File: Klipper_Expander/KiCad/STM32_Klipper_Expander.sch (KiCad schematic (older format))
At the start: 45 parts, among them J1 USB_B_Micro, J10 Conn_01x01, J11 Conn_01x03, J12 Conn_01x02, J2 Conn_01x04, J4 Conn_01x03, J5 Vin, J6 Screw_Terminal_01x08, J7 Conn_01x02, J8 Conn_01x02, J9 Conn_01x02, Q1 IRLML6344TRPBF, Q2 IRLML6344TRPBF, Q3 IRLML6344TRPBF, Q4 IRLML6344TRPBF, SW2 SW_SPST, U1 STM32F042F6Px, U2 AP2127K-3.3, U3 74LVC1G17

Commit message: Status LED's and silkscren adjustments.
Added status LED's for Vin (12/24V), USB (5V), and all 4 mosfets on the drain. LED's will signal mosfet output status.

Gerber and PNP files still need to be completed.
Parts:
- added D2, D3, D4, D5, D6, D7: LED, LED_SMD:LED_0805_2012Metric, symbol Device:LED
- added R15, R18, R19, R20, R22: 4.7K, Resistor_SMD:R_0805_2012Metric, symbol Device:R
- added R21: 1K, Resistor_SMD:R_0805_2012Metric, symbol Device:R
- J12: value Conn_01x02 -> Conn_01x03; footprint Connector_PinHeader_2.54mm:PinHeader_1x02_P2.54mm_Vertical -> Connector_PinHeader_2.54mm:PinHeader_1x03_P2.54mm_Vertical; symbol Connector_Generic:Conn_01x02 -> Connector_Generic:Conn_01x03
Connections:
- wire segments 140 -> 168

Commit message: Updated Gerber and Production files, Minor changes
Changed thermsitor pullups to 4K7 to increse range and reliability.
Added silkscreen to indicate what the status LED's are showing.
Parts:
- R16, R17: value 10K -> 4.7K; LCSC C17414 -> C17673; MPN RC0805JR-0710KL -> RC0805JR-074K7L; SKU 301010361 -> 301010306
- U3: footprint Package_TO_SOT_SMD:SOT-353_SC-70-5 -> digikey-footprints:SOT-753; LCSC C124293 -> C6076; MPN 74LVC1G17SE-7 -> (none)
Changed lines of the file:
@@
 F 0 "U3" H 5350 4000 50  0000 C CNN
 F 1 "74LVC1G17" H 5250 3650 50  0000 C CNN
-F 2 "Package_TO_SOT_SMD:SOT-353_SC-70-5" H 5550 3800 50  0001 C CNN
+F 2 "digikey-footprints:SOT-753" H 5550 3800 50  0001 C CNN
 F 3 "http://www.ti.com/lit/sg/scyt129e/scyt129e.pdf" H 5550 3800 50  0001 C CNN
-F 4 "C124293" H 5550 3800 50  0001 C CNN "LCSC"
-F 5 "74LVC1G17SE-7" H 5350 4100 50  0001 C CNN "MPN"
+F 4 "C6076" H 5550 3800 50  0001 C CNN "LCSC"
 	1    5550 3800
 	1    0    0    -1
@@
 	1    2650 6350
 	1    0    0    1
-$EndComp
-$Comp
-L Device:R R16
-U 1 1 5E341B23
-P 6750 5550
-F 0 "R16" H 6680 5504 50  0000 R CNN
-F 1 "10K" H 6680 5595 50  0000 R CNN
-F 2 "Resistor_SMD:R_0805_2012Metric" V 6680 5550 50  0001 C CNN
-F 3 "~" H 6750 5550 50  0001 C CNN
-F 4 "C17414" H 6750 5550 50  0001 C CNN "LCSC"
-F 5 "RC0805JR-0710KL" H 6680 5604 50  0001 C CNN "MPN"
-F 6 "301010361" H 6680 5604 50  0001 C CNN "SKU"
-	1    6750 5550
-	0    -1   1    0
-$EndComp
-$Comp
-L Device:R R17
-U 1 1 5E34C47F
-P 8000 5550
-F 0 "R17" H 7930 5504 50  0000 R CNN
-F 1 "10K" H 7930 5595 50  0000 R CNN
-F 2 "Resistor_SMD:R_0805_2012Metric" V 7930 5550 50  0001 C CNN
-F 3 "~" H 8000 5550 50  0001 C CNN
-F 4 "C17414" H 8000 5550 50  0001 C CNN "LCSC"
-F 5 "RC0805JR-0710KL" H 7930 5604 50  0001 C CNN "MPN"
-F 6 "301010361" H 7930 5604 50  0001 C CNN "SKU"
-	1    8000 5550
-	0    -1   1    0
 $EndComp
 $Comp
@@
 	4050 3200 4050 3150
 $Comp
-L power:+3V3 #PWR?
+L power:+3V3 #PWR0110
 U 1 1 5EBA479A
 P 3800 5500
-F 0 "#PWR?" H 3800 5350 50  0001 C CNN
+F 0 "#PWR0110" H 3800 5350 50  0001 C CNN
 F 1 "+3V3" H 3815 5673 50  0000 C CNN
 F 2 "" H 3800 5500 50  0001 C CNN
@@
 Wire Wire Line
 	3800 5600 3800 5500
+$Comp
+L Device:R R16
+U 1 1 5E9F90AA
+P 6750 5550
+F 0 "R16" H 6680 5504 50  0000 R CNN
+F 1 "4.7K" H 6680 5595 50  0000 R CNN
+F 2 "Resistor_SMD:R_0805_2012Metric" V 6680 5550 50  0001 C CNN
+F 3 "~" H 6750 5550 50  0001 C CNN
+F 4 "C17673" H 6750 5550 50  0001 C CNN "LCSC"
+F 5 "RC0805JR-074K7L" H 6750 5550 50  0001 C CNN "MPN"
+F 6 "301010306" H 6750 5550 50  0001 C CNN "SKU"
+	1    6750 5550
+	0    -1   1    0
+$EndComp
+$Comp
+L Device:R R17
+U 1 1 5EA00768
+P 8000 5550
+F 0 "R17" H 7930 5504 50  0000 R CNN
+F 1 "4.7K" H 7930 5595 50  0000 R CNN
+F 2 "Resistor_SMD:R_0805_2012Metric" V 7930 5550 50  0001 C CNN
+F 3 "~" H 8000 5550 50  0001 C CNN
+F 4 "C17673" H 8000 5550 50  0001 C CNN "LCSC"
+F 5 "RC0805JR-074K7L" H 8000 5550 50  0001 C CNN "MPN"
+F 6 "301010306" H 8000 5550 50  0001 C CNN "SKU"
+	1    8000 5550
+	0    -1   1    0
+$EndComp
 $EndSCHEMATC

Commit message: Add interactive BOM and Project Based Library (#12)
* Change from global to Project based library

Project based libraary added which includes all schematic symbols, footprints, and 3D models

* Fixed links to Footprint and Symbol Libraries

* Add interactiveBOM
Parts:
- C1, C2, C3, C4, C5, C6: footprint Capacitor_SMD:C_0805_2012Metric -> KlipperExpander:C_0805_2012Metric; symbol Device:C -> KlipperExpander:C
- D1, D2, D3, D4, D5, D6, D7: footprint LED_SMD:LED_0805_2012Metric -> KlipperExpander:LED_0805_2012Metric; symbol Device:LED -> KlipperExpander:LED
- F1: footprint TRA_KiCad_Footprints:3544-2_FuseHolder -> KlipperExpander:3544-2_FuseHolder; symbol Device:Fuse -> KlipperExpander:Fuse
- H1, H2: footprint MountingHole:MountingHole_3.2mm_M3 -> KlipperExpander:MountingHole_3.2mm_M3
- J1: footprint TRA_KiCad_Footprints:Molex-105017-0001-USBMicroB -> KlipperExpander:Molex-105017-0001-USBMicroB; symbol Connector:USB_B_Micro -> KlipperExpander:USB_B_Micro
- J10: footprint Connector_PinHeader_2.54mm:PinHeader_1x01_P2.54mm_Vertical -> KlipperExpander:PinHeader_1x01_P2.54mm_Vertical; symbol Connector_Generic:Conn_01x01 -> KlipperExpander:Conn_01x01
- J11, J12, J4: footprint Connector_PinHeader_2.54mm:PinHeader_1x03_P2.54mm_Vertical -> KlipperExpander:PinHeader_1x03_P2.54mm_Vertical; symbol Connector_Generic:Conn_01x03 -> KlipperExpander:Conn_01x03
- J2: footprint Connector_PinHeader_2.54mm:PinHeader_1x04_P2.54mm_Vertical -> KlipperExpander:PinHeader_1x04_P2.54mm_Vertical; symbol Connector_Generic:Conn_01x04 -> KlipperExpander:Conn_01x04
- J5: footprint TRA_KiCad_Footprints:1x02_ScrewTerminal_Phoenix -> KlipperExpander:1x02_ScrewTerminal_Phoenix; symbol Connector:Screw_Terminal_01x02 -> KlipperExpander:Screw_Terminal_01x02
- J6: footprint TRA_KiCad_Footprints:TerminalBlock_Phoenix_MKDS-1,5-8-5.08_1x08_P5.08mm_Horizontal -> KlipperExpander:1x08_ScrewTerminal_Phoenix; symbol Connector:Screw_Terminal_01x08 -> KlipperExpander:Screw_Terminal_01x08
- J7: footprint Connector_PinHeader_2.54mm:PinHeader_1x02_P2.54mm_Vertical -> KlipperExpander:PinHeader_1x02_P2.54mm_Vertical; symbol Connector_Generic:Conn_01x02 -> KlipperExpander:Conn_01x02
- J8, J9: footprint Connector_JST:JST_XH_B02B-XH-A_1x02_P2.50mm_Vertical -> KlipperExpander:PinHeader_1x02_P2.54mm_Vertical; symbol Connector_Generic:Conn_01x02 -> KlipperExpander:Conn_01x02
- Q1, Q2, Q3, Q4: footprint Package_TO_SOT_SMD:SOT-23 -> KlipperExpander:SOT-23; symbol dk_Transistors-FETs-MOSFETs-Single:IRLML6344TRPBF -> KlipperExpander:IRLML6344TRPBF
- R1, R10, R11, R12, R13, R14, R15, R16, R17, R18, R19, R2, R20, R21, R22, R3, R4, R5, R6, R7, R8, R9: footprint Resistor_SMD:R_0805_2012Metric -> KlipperExpander:R_0805_2012Metric; symbol Device:R -> KlipperExpander:R
- SW2: footprint TRA_KiCad_Footprints:2PinTactileButton -> KlipperExpander:2PinTactileButton; symbol Switch:SW_SPST -> KlipperExpander:SW_SPST
- U1: footprint Package_SO:TSSOP-20_4.4x6.5mm_P0.65mm -> KlipperExpander:TSSOP-20_4.4x6.5mm_P0.65mm; symbol MCU_ST_STM32F0:STM32F042F6Px -> KlipperExpander:STM32F042F6Px
- U2: footprint Package_TO_SOT_SMD:SOT-23-5 -> KlipperExpander:SOT-23-5; symbol Regulator_Linear:AP2127K-3.3 -> KlipperExpander:AP2127K-3.3
- U3: footprint digikey-footprints:SOT-753 -> KlipperExpander:SOT-753; symbol 74xGxx:74LVC1G17 -> KlipperExpander:74LVC1G17

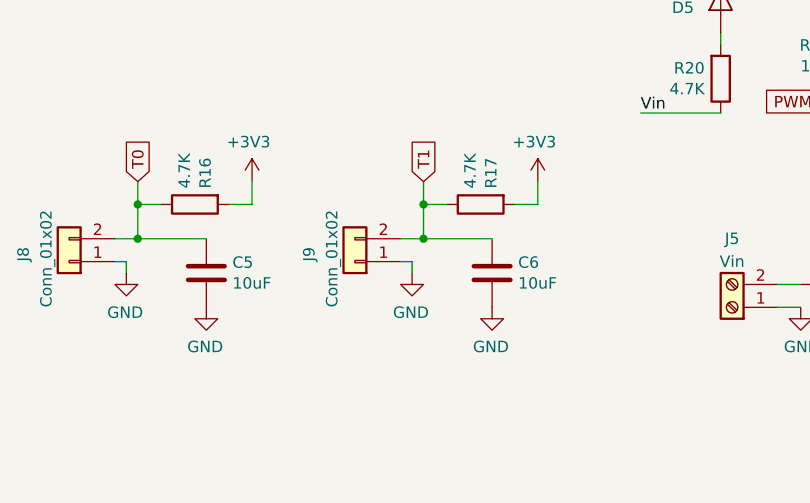
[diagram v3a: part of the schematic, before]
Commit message: Silkscreen adjustment and capacitro simplifications
Changed C5 and C6 from 10uF to 4.7uF for part simplification.

Change silkscreen sizings for better printing
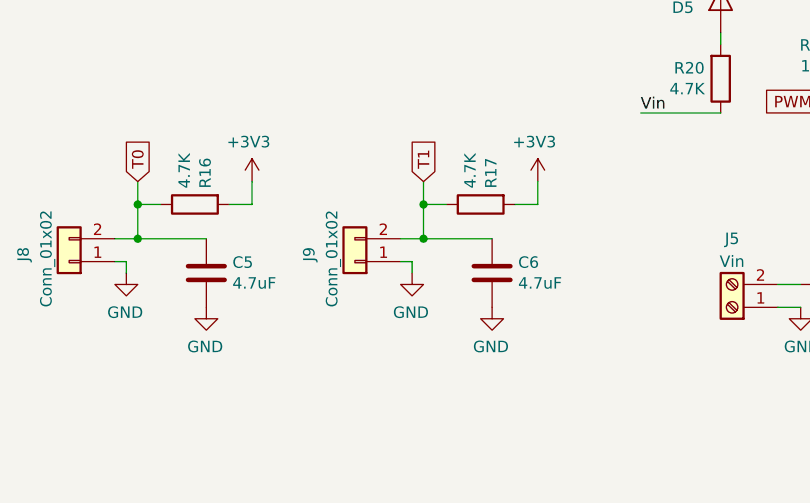
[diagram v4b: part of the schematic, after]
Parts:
- C5, C6: value 10uF -> 4.7uF; LCSC C15850 -> C1779; MPN CC0805ZKY5V6BB106 -> CC0805KKX5R8BB475; SKU 302010158 -> 302010146
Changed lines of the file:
@@
 P 6800 5850
 F 0 "C5" H 6914 5804 50  0000 L CNN
-F 1 "10uF" H 6914 5895 50  0000 L CNN
+F 1 "4.7uF" H 6914 5895 50  0000 L CNN
 F 2 "KlipperExpander:C_0805_2012Metric" H 6838 5700 50  0001 C CNN
 F 3 "~" H 6800 5850 50  0001 C CNN
-F 4 "C15850" H 6800 5850 50  0001 C CNN "LCSC"
-F 5 "CC0805ZKY5V6BB106 " H 6914 5904 50  0001 C CNN "MPN"
-F 6 "302010158" H 6914 5904 50  0001 C CNN "SKU"
+F 4 "C1779" H 6800 5850 50  0001 C CNN "LCSC"
+F 5 "CC0805KKX5R8BB475" H 6914 5904 50  0001 C CNN "MPN"
+F 6 "302010146" H 6914 5904 50  0001 C CNN "SKU"
 	1    6800 5850
 	1    0    0    1
@@
 P 8050 5850
 F 0 "C6" H 8164 5804 50  0000 L CNN
-F 1 "10uF" H 8164 5895 50  0000 L CNN
+F 1 "4.7uF" H 8164 5895 50  0000 L CNN
 F 2 "KlipperExpander:C_0805_2012Metric" H 8088 5700 50  0001 C CNN
 F 3 "~" H 8050 5850 50  0001 C CNN
-F 4 "C15850" H 8050 5850 50  0001 C CNN "LCSC"
-F 5 "CC0805ZKY5V6BB106 " H 8164 5904 50  0001 C CNN "MPN"
-F 6 "302010158" H 8164 5904 50  0001 C CNN "SKU"
+F 4 "C1779" H 8050 5850 50  0001 C CNN "LCSC"
+F 5 "CC0805KKX5R8BB475" H 8164 5904 50  0001 C CNN "MPN"
+F 6 "302010146" H 8164 5904 50  0001 C CNN "SKU"
 	1    8050 5850
 	1    0    0    1
